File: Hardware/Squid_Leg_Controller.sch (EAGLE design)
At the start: 10 parts, among them IC1 REG1117, J1 SPI_PRG, Q1 MMBT2222A

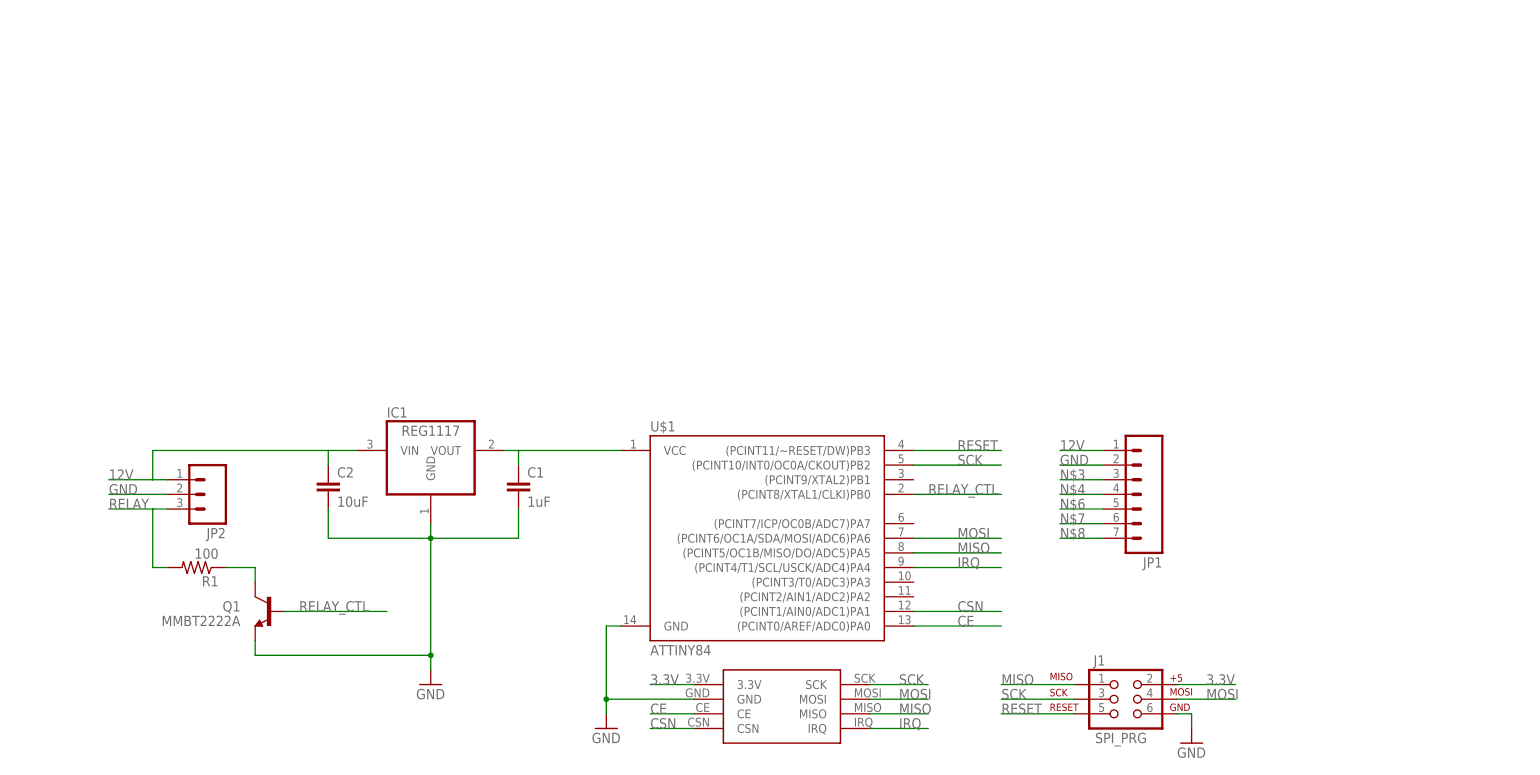
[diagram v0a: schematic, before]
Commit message: saving progress on adding in buzzer and led controls
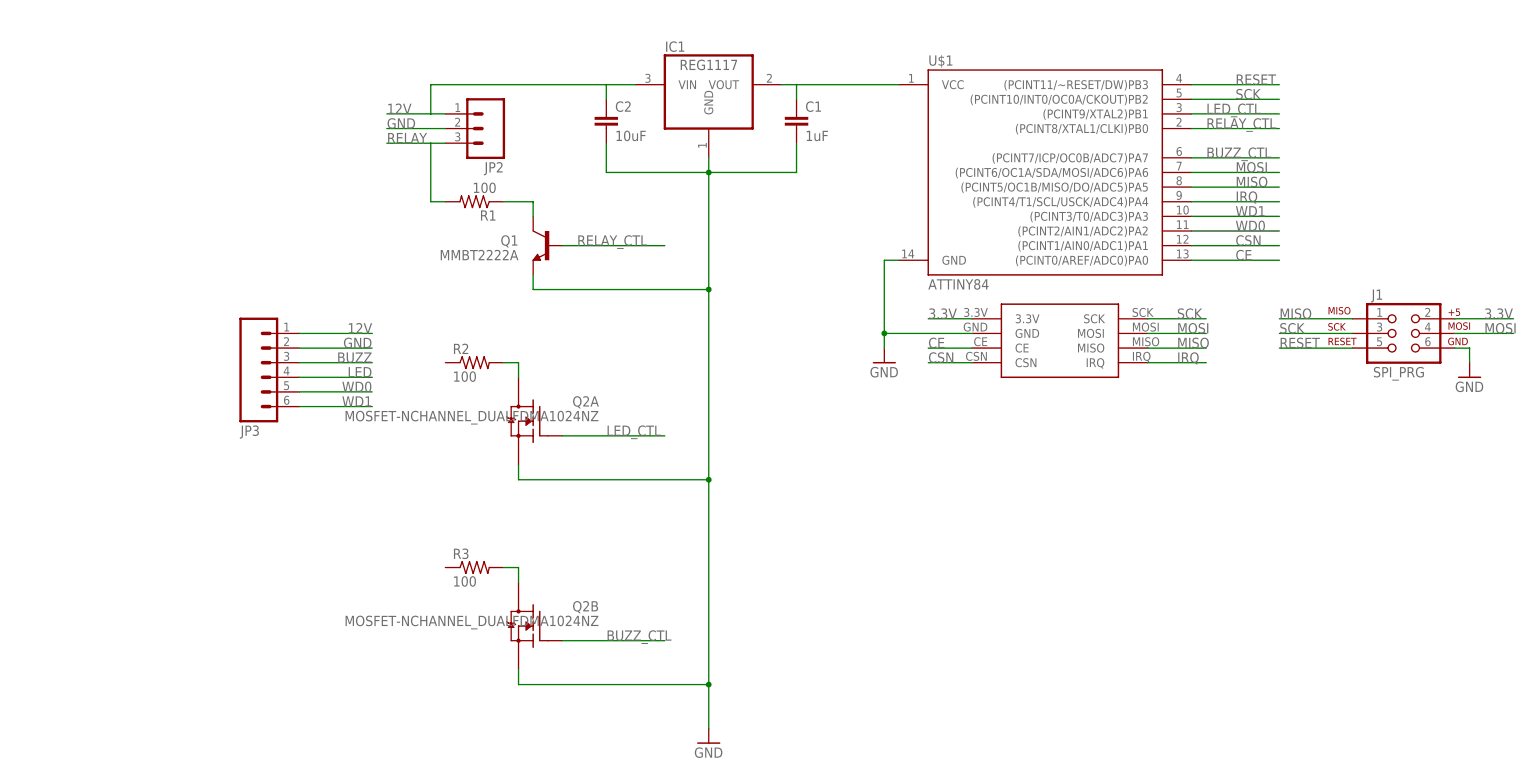
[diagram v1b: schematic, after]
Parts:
- removed JP1: (no value), SparkFun-Connectors:M07LOCK
- removed U$3: NRF24L01+_MODULE, Dan9186 - RF:NRF24L01+_MODULE
- added JP3: (no value), SparkFun-Connectors:M06LOCK
- added Q2: MOSFET-NCHANNEL_DUALFDMA1024NZ, SparkFun-DiscreteSemi:MOSFET-NCHANNEL_DUALFDMA1024NZ
- added R2, R3: 100, resistor:R-US_M0805
- added U$4: NRF24L01+, Derp - RF:NRF24L01+_MODULEOFF_BOARD
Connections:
- removed net N$3: JP1.3
- removed net N$4: JP1.4
- removed net N$6: JP1.5
- removed net N$7: JP1.6
- removed net N$8: JP1.7
- new net BUZZ: JP3.3
- new net BUZZ_CTL: Q2B.G, U$1.(PCINT7/ICP/OC0B/ADC7)PA7
- new net LED: JP3.4
- new net LED_CTL: Q2A.G, U$1.(PCINT9/XTAL2)PB1
- new net N$1: Q2A.D1, R2.2
- new net N$2: Q2B.D1, R3.2
- new net WD0: JP3.5, U$1.(PCINT2/AIN1/ADC2)PA2
- new net WD1: JP3.6, U$1.(PCINT3/T0/ADC3)PA3
- net 12V: now also JP3.1; no longer JP1.1
- net 3.3V: now also U$4.3.3V; no longer U$3.3.3V
- net CE: now also U$4.CE; no longer U$3.CE
- net CSN: now also U$4.CSN; no longer U$3.CSN
- net GND: now also JP3.2, Q2A.S, Q2B.S, U$4.GND; no longer JP1.2, U$3.GND
- net IRQ: now also U$4.IRQ; no longer U$3.IRQ
- net MISO: now also U$4.MISO; no longer U$3.MISO
- net MOSI: now also U$4.MOSI; no longer U$3.MOSI
- net SCK: now also U$4.SCK; no longer U$3.SCK
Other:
- moved on the sheet: C1, C2, IC1, J1, JP2, Q1, R1, U$1

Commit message: routed remainig pieces, added in mosfet to control LED and buzzer, and attached DRU
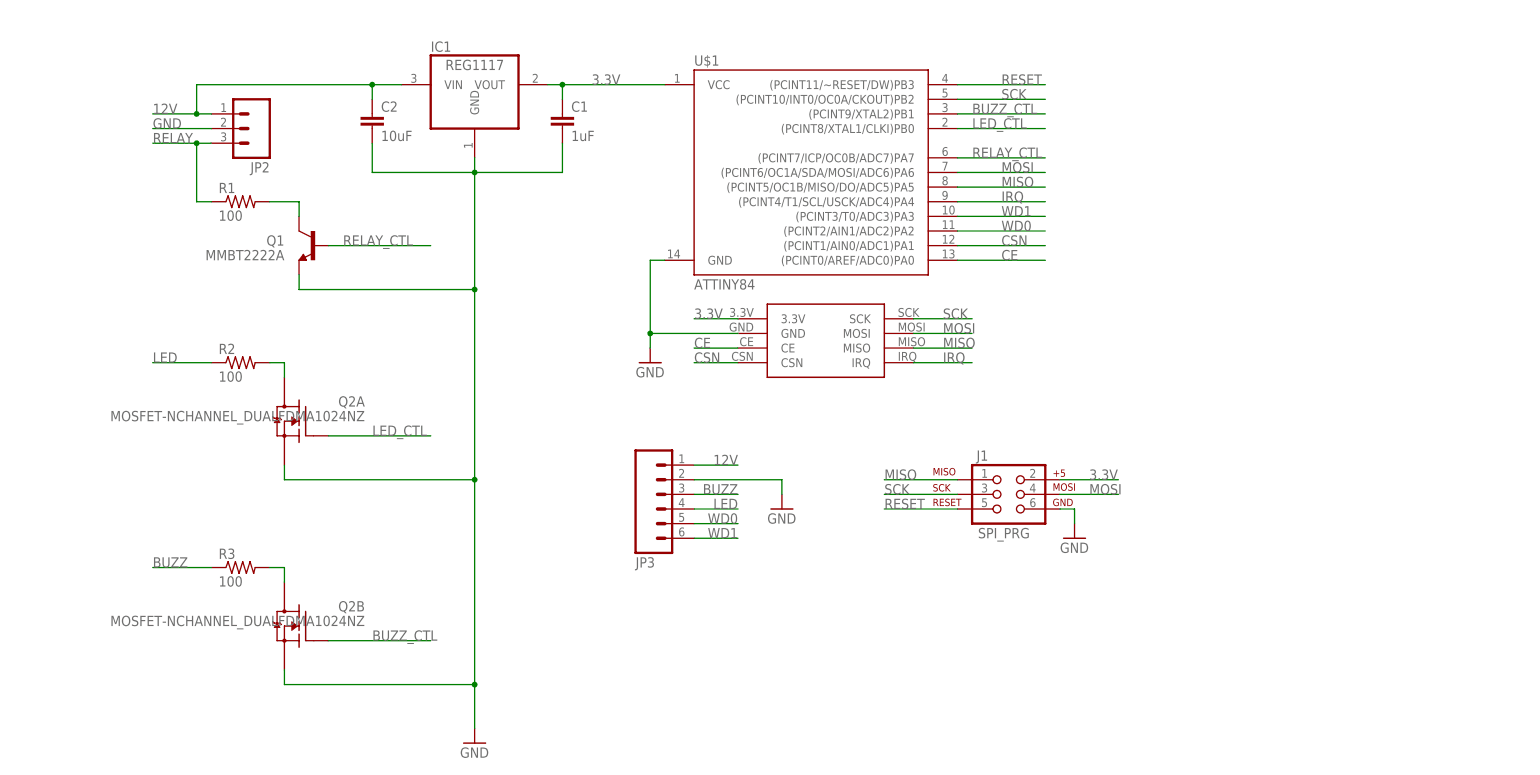
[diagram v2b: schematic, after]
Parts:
- R1, R2, R3: device resistor:R-US_M0805 -> resistor:R-US_R0805
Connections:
- net BUZZ: now also R3.1
- net BUZZ_CTL: now also U$1.(PCINT9/XTAL2)PB1; no longer U$1.(PCINT7/ICP/OC0B/ADC7)PA7
- net LED: now also R2.1
- net LED_CTL: now also U$1.(PCINT8/XTAL1/CLKI)PB0; no longer U$1.(PCINT9/XTAL2)PB1
- net N$5: now also R1.2; no longer R1.1
- net RELAY: now also R1.1; no longer R1.2
- net RELAY_CTL: now also U$1.(PCINT7/ICP/OC0B/ADC7)PA7; no longer U$1.(PCINT8/XTAL1/CLKI)PB0
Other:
- moved on the sheet: C1, C2, IC1, J1, JP2, JP3, Q1, Q2A, Q2B, R1, R2, R3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

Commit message: updated missing resistors and removed traces on board, tracing needs to be redone
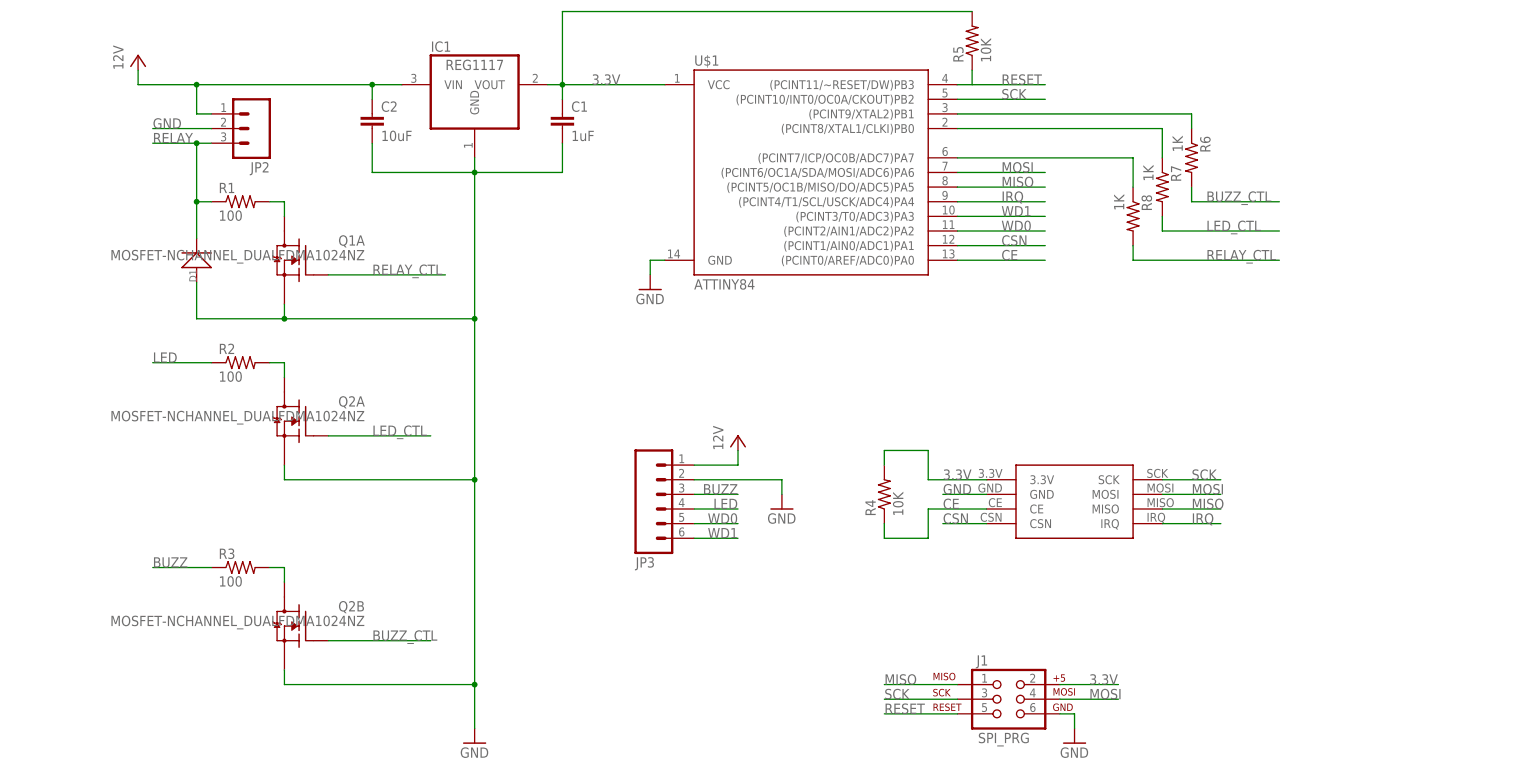
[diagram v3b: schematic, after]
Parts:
- added D1: (no value), OPL Eagle Library:D-SMA
- added R4, R5: 10K, resistor:R-US_R0603
- added R6, R7, R8: 1K, resistor:R-US_R0603
- Q1: value MMBT2222A -> MOSFET-NCHANNEL_DUALFDMA1024NZ; device SparkFun-DiscreteSemi:TRANSISTOR_NPNMMBT2222A -> SparkFun-DiscreteSemi:MOSFET-NCHANNEL_DUALFDMA1024NZ
- R1, R2, R3: device resistor:R-US_R0805 -> resistor:R-US_R0603
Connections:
- net 12V renamed VCC
- new net N$3: R6.1, U$1.(PCINT9/XTAL2)PB1
- new net N$4: R7.1, U$1.(PCINT8/XTAL1/CLKI)PB0
- new net N$8: R8.1, U$1.(PCINT7/ICP/OC0B/ADC7)PA7
- net 3.3V: now also R4.2, R5.2
- net BUZZ_CTL: now also R6.2; no longer U$1.(PCINT9/XTAL2)PB1
- net CE: now also R4.1
- net GND: now also D1.+, Q1A.S; no longer Q1.E
- net LED_CTL: now also R7.2; no longer U$1.(PCINT8/XTAL1/CLKI)PB0
- net N$5: now also Q1A.D1; no longer Q1.C
- net RELAY: now also D1.-
- net RELAY_CTL: now also Q1A.G, R8.2; no longer Q1.B, U$1.(PCINT7/ICP/OC0B/ADC7)PA7
- net RESET: now also R5.1
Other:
- moved on the sheet: J1

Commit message: added button and rerouted board
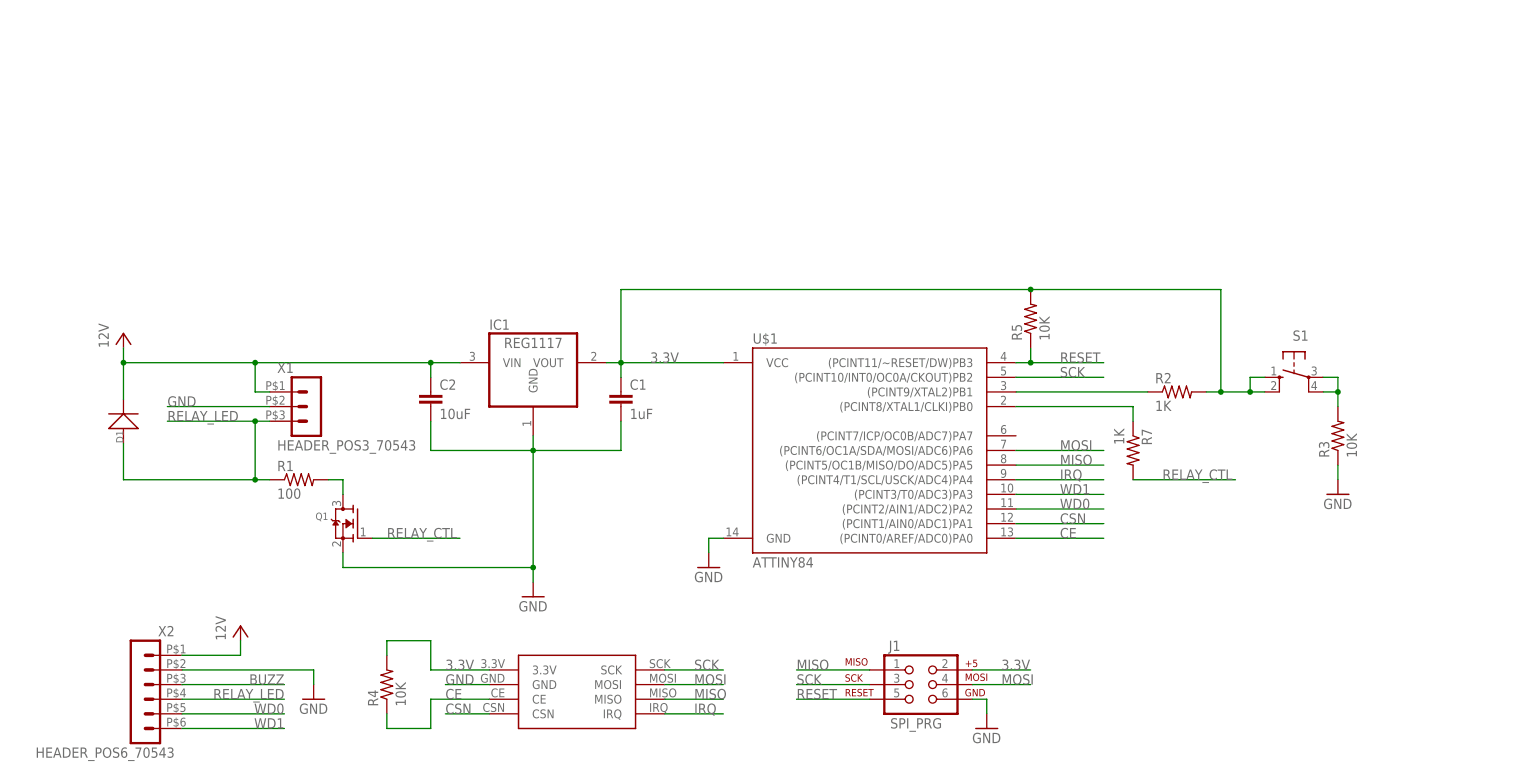
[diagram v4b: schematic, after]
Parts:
- removed JP2: (no value), SparkFun-Connectors:M03LOCK
- removed JP3: (no value), SparkFun-Connectors:M06LOCK
- removed Q2: MOSFET-NCHANNEL_DUALFDMA1024NZ, SparkFun-DiscreteSemi:MOSFET-NCHANNEL_DUALFDMA1024NZ
- removed R6, R8: 1K, resistor:R-US_R0603
- added S1: (no value), switch-omron:10-XX
- added X1: HEADER_POS3_70543, Derp - Connectors - Molex SL:HEADER_POS3_70543
- added X2: HEADER_POS6_70543, Derp - Connectors - Molex SL:HEADER_POS6_70543
- Q1: value MOSFET-NCHANNEL_DUALFDMA1024NZ -> (none); device SparkFun-DiscreteSemi:MOSFET-NCHANNEL_DUALFDMA1024NZ -> adafruit:MOSFET-NREFLOW
- R2: value 100 -> 1K
- R3: value 100 -> 10K
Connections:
- removed net BUZZ_CTL: Q2B.G, R6.2
- removed net LED: JP3.4, R2.1
- removed net LED_CTL: Q2A.G, R7.2
- removed net N$3: R6.1, U$1.(PCINT9/XTAL2)PB1
- removed net N$8: R8.1, U$1.(PCINT7/ICP/OC0B/ADC7)PA7
- removed net RELAY: D1.-, JP2.3, R1.1
- new net RELAY_LED: D1.+, R1.1, X1.3, X2.4
- net 3.3V: now also R2.2, S1.S, S1.S1
- net BUZZ: now also X2.3; no longer JP3.3, R3.1
- net GND: now also Q1.S, R3.1, X1.2, X2.2; no longer D1.+, JP2.2, JP3.2, Q1A.S, Q2A.S, Q2B.S
- net N$1: now also R2.1, U$1.(PCINT9/XTAL2)PB1; no longer Q2A.D1, R2.2
- net N$2: now also S1.P, S1.P1; no longer Q2B.D1
- net N$5: now also Q1.D; no longer Q1A.D1
- net RELAY_CTL: now also Q1.G, R7.2; no longer Q1A.G, R8.2
- net VCC: now also D1.-, X1.1, X2.1; no longer JP2.1, JP3.1
- net WD0: now also X2.5; no longer JP3.5
- net WD1: now also X2.6; no longer JP3.6
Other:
- moved on the sheet: C1, C2, D1, IC1, J1, R1, R2, R3, R4, R5, R7, U$1
